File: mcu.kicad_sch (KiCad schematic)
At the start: 18 parts, among them J11 Conn_ARM_JTAG_SWD_10, SW1 SW_Push, U3 ATSAMD21J18A-A, Y1 32.768kHz

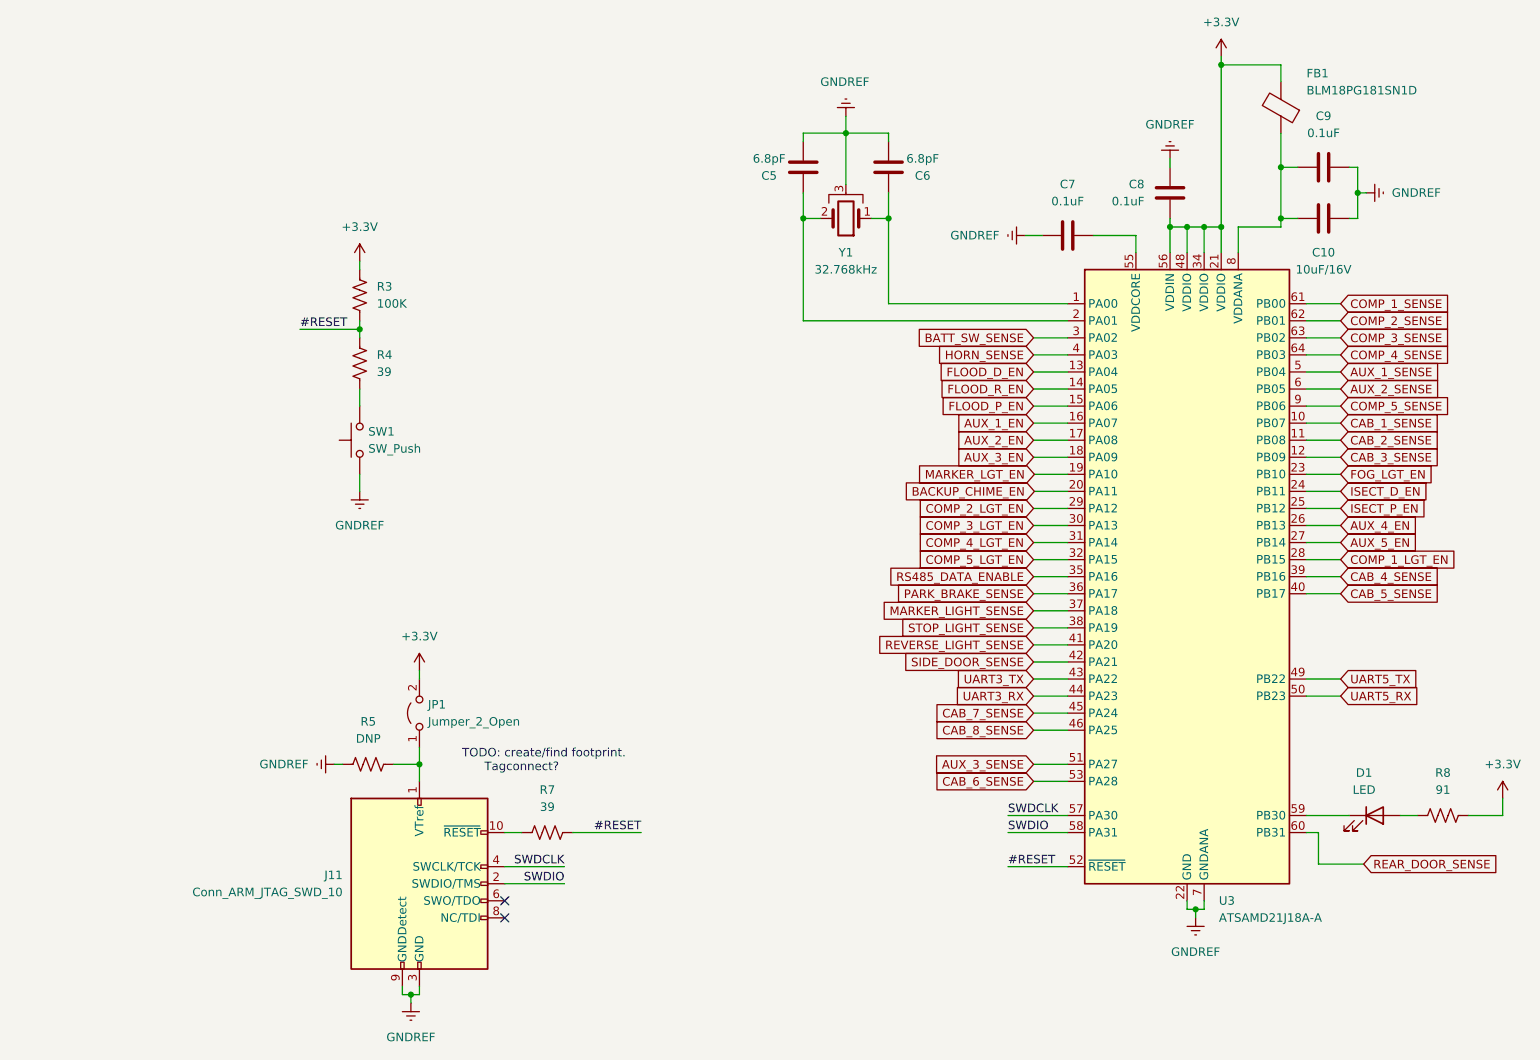
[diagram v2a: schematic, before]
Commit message: add IO expander and additional AUX outputs
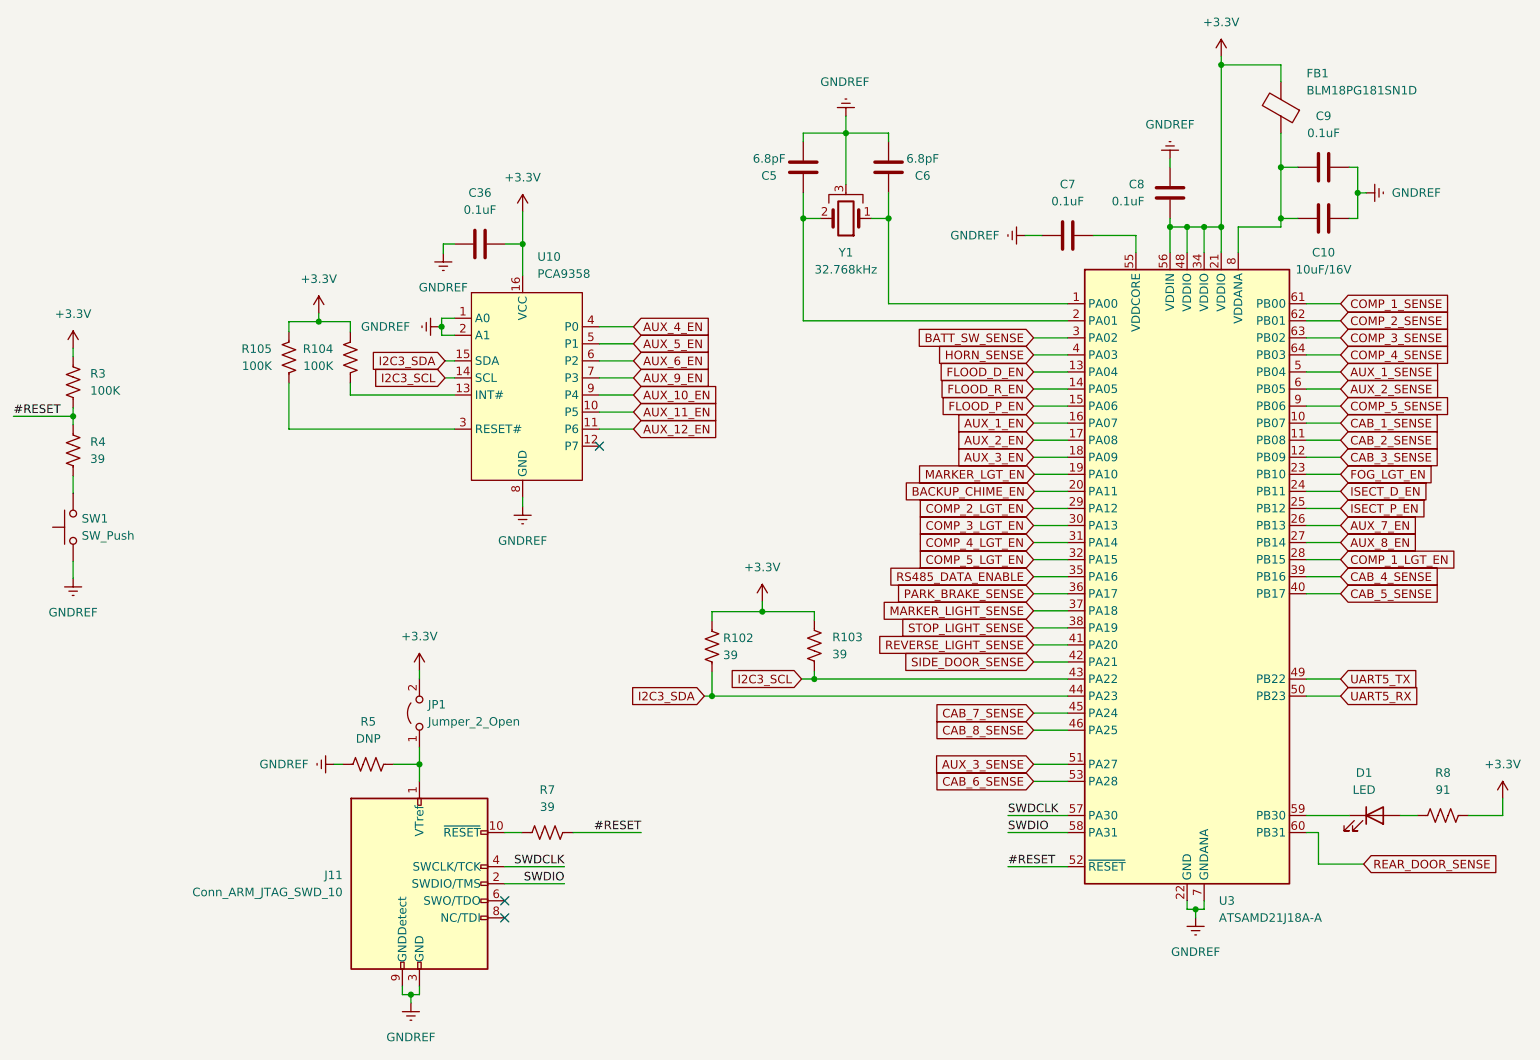
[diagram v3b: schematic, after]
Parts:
- added C36: 0.1uF, Capacitor_SMD:C_0805_2012Metric_Pad1.18x1.45mm_HandSolder, symbol Device:C
- added R102, R103: 39, Resistor_SMD:R_0805_2012Metric_Pad1.20x1.40mm_HandSolder, symbol Device:R_US
- added R104, R105: 100K, Resistor_SMD:R_0805_2012Metric_Pad1.20x1.40mm_HandSolder, symbol Device:R_US
- added U10: PCA9358, Package_SO:SOIC-16W_7.5x10.3mm_P1.27mm, symbol Toadly:PCA9358
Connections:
- net +3.3V: now also C36.1, R102.2, R103.2, R104.2, R105.2, U10.16 (VCC)
- net AUX_4_EN: now also U10.4 (P0); no longer U3.26 (PB13)
- net AUX_5_EN: now also U10.5 (P1); no longer U3.27 (PB14)
- net GNDREF: now also C36.2, U10.1 (A0), U10.2 (A1), U10.8 (GND)
- net UART3_RX renamed I2C3_SDA
- net I2C3_SDA: now also R102.1, U10.15 (SDA)
- net UART3_TX renamed I2C3_SCL
- net I2C3_SCL: now also R103.1, U10.14 (SCL)
- new net: R105.1, U10.3 (RESET#)
- new net: R104.1, U10.13 (INT#)
- new net AUX_10_EN: U10.9 (P4)
- new net AUX_11_EN: U10.10 (P5)
- new net AUX_12_EN: U10.11 (P6)
- new net AUX_6_EN: U10.6 (P2)
- new net AUX_7_EN: U3.26 (PB13)
- new net AUX_8_EN: U3.27 (PB14)
- new net AUX_9_EN: U10.7 (P3)
- no-connect marks 2 -> 3
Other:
- note removed: "TODO: create/find footprint. Tagconnect?"
- moved on the sheet: R3, R4, SW1

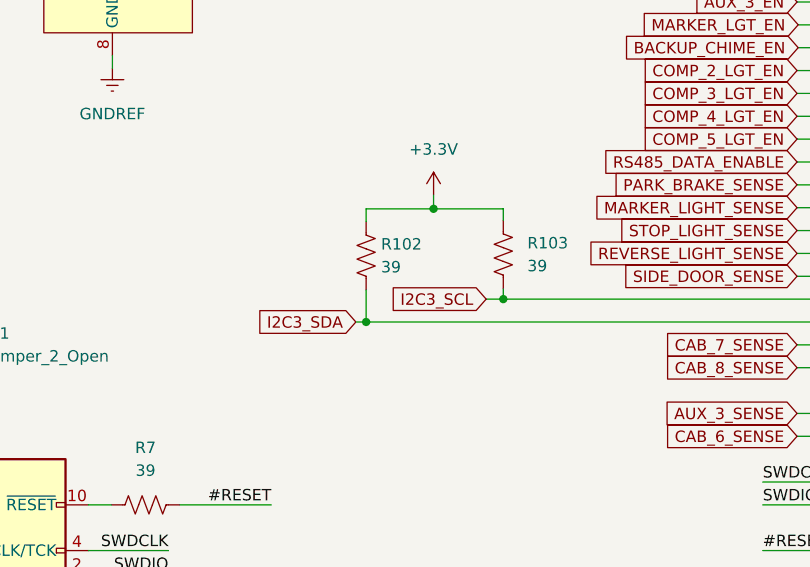
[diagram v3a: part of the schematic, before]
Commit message: generate pedigree B
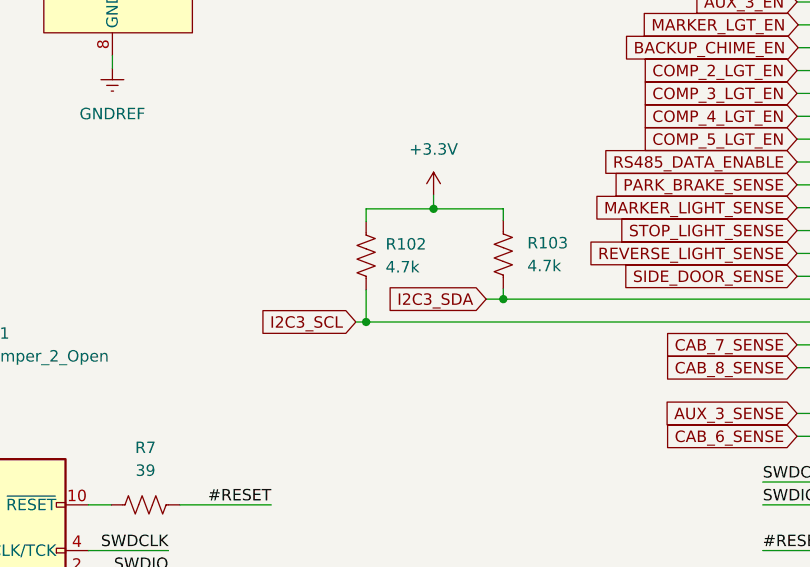
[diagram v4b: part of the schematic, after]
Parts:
- R102, R103: value 39 -> 4.7k
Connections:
- net I2C3_SCL: now also R102.1, U3.44 (PA23); no longer R103.1, U3.43 (PA22)
- net I2C3_SDA: now also R103.1, U3.43 (PA22); no longer R102.1, U3.44 (PA23)
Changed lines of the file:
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@@
     )
   )
-  (global_label "I2C3_SDA" (shape input) (at 124.968 120.65 180) (fields_autoplaced)
-    (effects (font (size 1.27 1.27)) (justify right))
-    (property "Intersheetrefs" "${INTERSHEET_REFS}" (at 113.1533 120.65 0)
+  (global_label "I2C3_SDA" (shape input) (at 139.446 118.11 180) (fields_autoplaced)
+    (effects (font (size 1.27 1.27)) (justify right))
+    (property "Intersheetrefs" "${INTERSHEET_REFS}" (at 127.6313 118.11 0)
       (effects (font (size 1.27 1.27)) (justify right) hide)
     )
@@
     )
   )
-  (global_label "I2C3_SCL" (shape input) (at 139.446 118.11 180) (fields_autoplaced)
-    (effects (font (size 1.27 1.27)) (justify right))
-    (property "Intersheetrefs" "${INTERSHEET_REFS}" (at 127.6918 118.11 0)
+  (global_label "I2C3_SCL" (shape input) (at 124.968 120.65 180) (fields_autoplaced)
+    (effects (font (size 1.27 1.27)) (justify right))
+    (property "Intersheetrefs" "${INTERSHEET_REFS}" (at 113.2138 120.65 0)
       (effects (font (size 1.27 1.27)) (justify right) hide)
     )
@@
       (effects (font (size 1.27 1.27)) (justify right))
     )
-    (property "Value" "39" (at 144.018 114.427 0)
+    (property "Value" "4.7k" (at 144.018 114.427 0)
       (effects (font (size 1.27 1.27)) (justify right))
     )
@@
   (symbol (lib_id "Device:R_US") (at 126.111 113.284 180) (unit 1)
     (in_bom yes) (on_board yes) (dnp no) (fields_autoplaced)
-    (property "Reference" "R102" (at 127.762 112.014 0)
-      (effects (font (size 1.27 1.27)) (justify right))
-    )
-    (property "Value" "39" (at 127.762 114.554 0)
-      (effects (font (size 1.27 1.27)) (justify right))
-    )
+    (property "Reference" "R102" (at 128.27 112.014 0)
+      (effects (font (size 1.27 1.27)) (justify right))
+    )
+    (property "Value" "4.7k" (at 128.27 114.554 0)
+      (effects (font (size 1.27 1.27)) (justify right))
+    )
